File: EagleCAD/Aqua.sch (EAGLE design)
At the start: 13 parts, among them IC1 TINY13-20PU, Q1 IRF3704

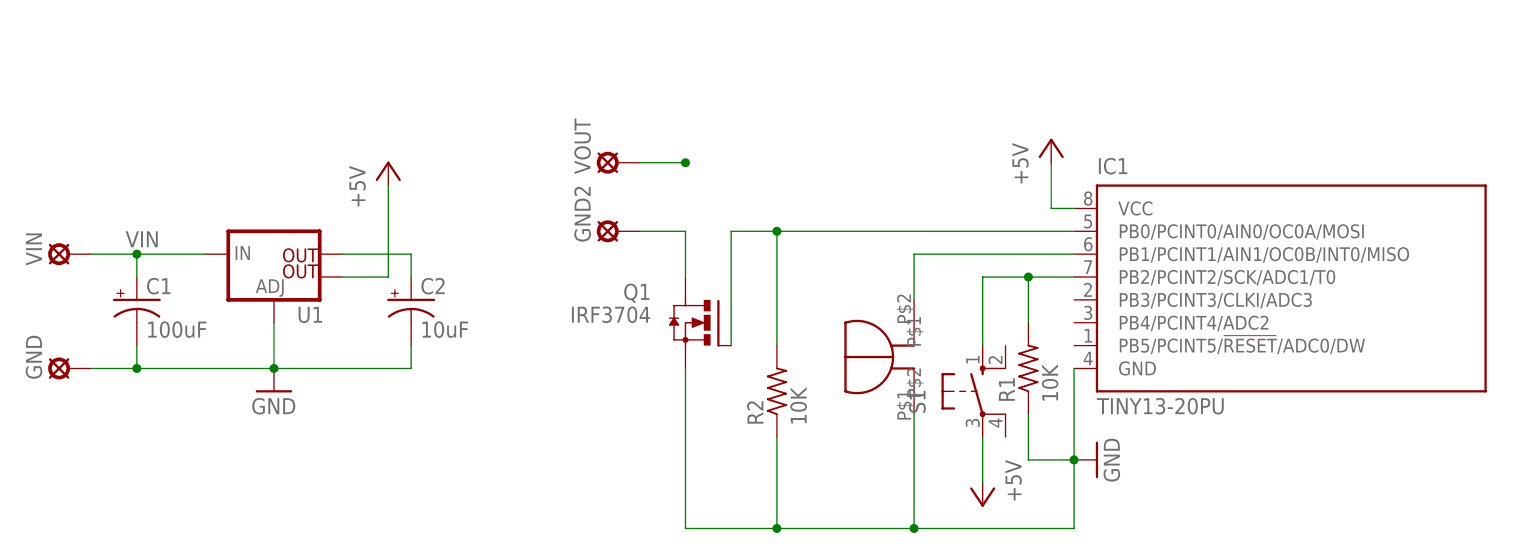
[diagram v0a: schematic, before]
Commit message: Time count improvement
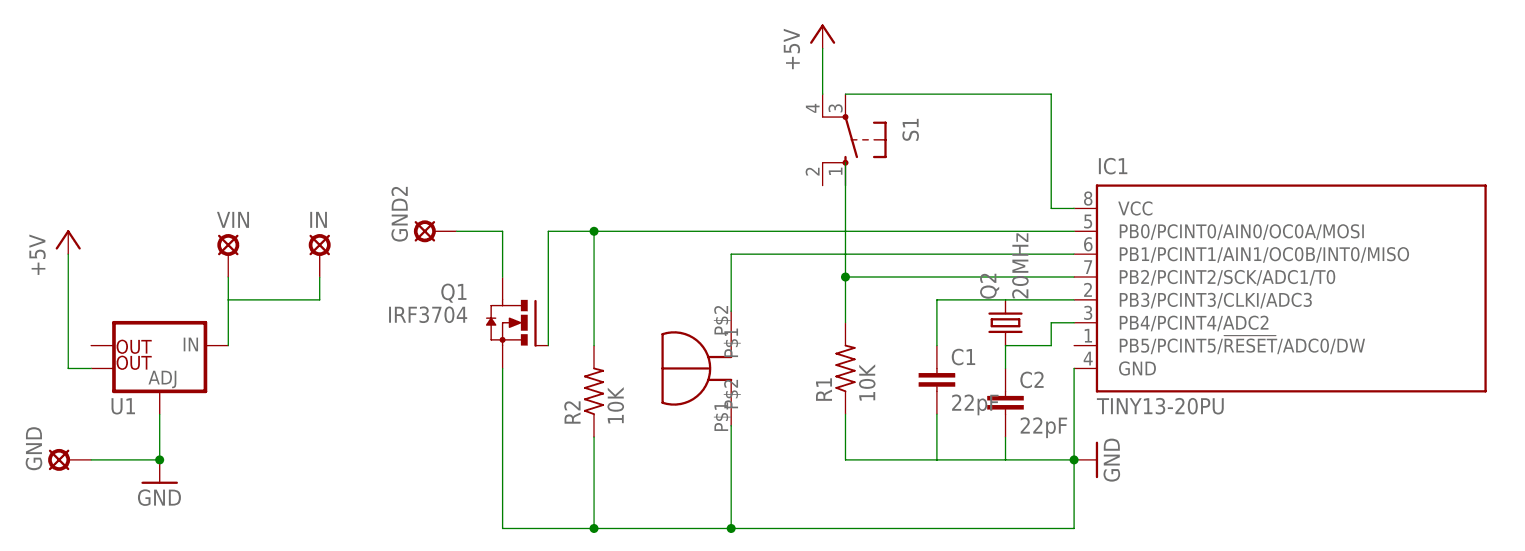
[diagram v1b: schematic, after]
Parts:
- removed VOUT: LSP11, solpad:LSP11
- added IN: LSP11, solpad:LSP11
- added Q2: 20MHz, adafruit:CRYSTALHC49U-V
- C1: value 100uF -> 22pF; device SparkFun-Capacitors:CAP_POLPTH2 -> capacitor-wima:C5/2.5
- C2: value 10uF -> 22pF; device SparkFun-Capacitors:CAP_POLPTH2 -> capacitor-wima:C5/2.5
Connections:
- removed net OUT: C2.+, U1.OUT
- removed net VIN: C1.+, U1.IN, VIN.MP, VOUT.MP
- new net N$3: C1.1, IC1.PB3/PCINT3/CLKI/ADC3, Q2.2
- new net N$6: C2.1, IC1.PB4/PCINT4/ADC2, Q2.1
- new net N$7: IC1.VCC, S1.P
- new net N$8: IN.MP, U1.IN, VIN.MP
- net +5V: now also S1.P1; no longer IC1.VCC, S1.P
- net GND: now also C1.2, C2.2; no longer C1.-, C2.-
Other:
- moved on the sheet: GND, GND2, Q1, R1, R2, S1, U1, VIN
